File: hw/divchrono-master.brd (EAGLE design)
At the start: 100 x 80 mm, 16 parts, among them U1 TPS562200DDCR

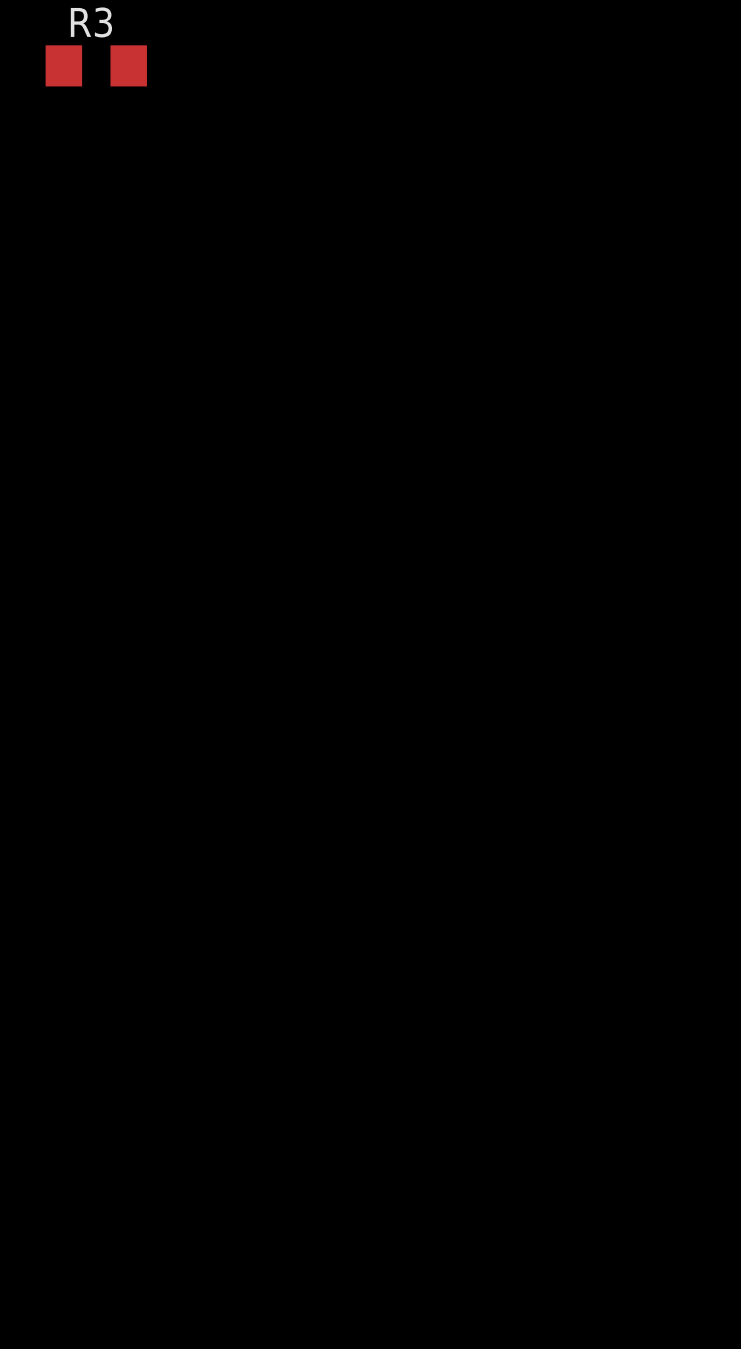
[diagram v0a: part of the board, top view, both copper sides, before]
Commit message: Added Nixie tube boost converter into schematic, library, and updated documentation for new layout.
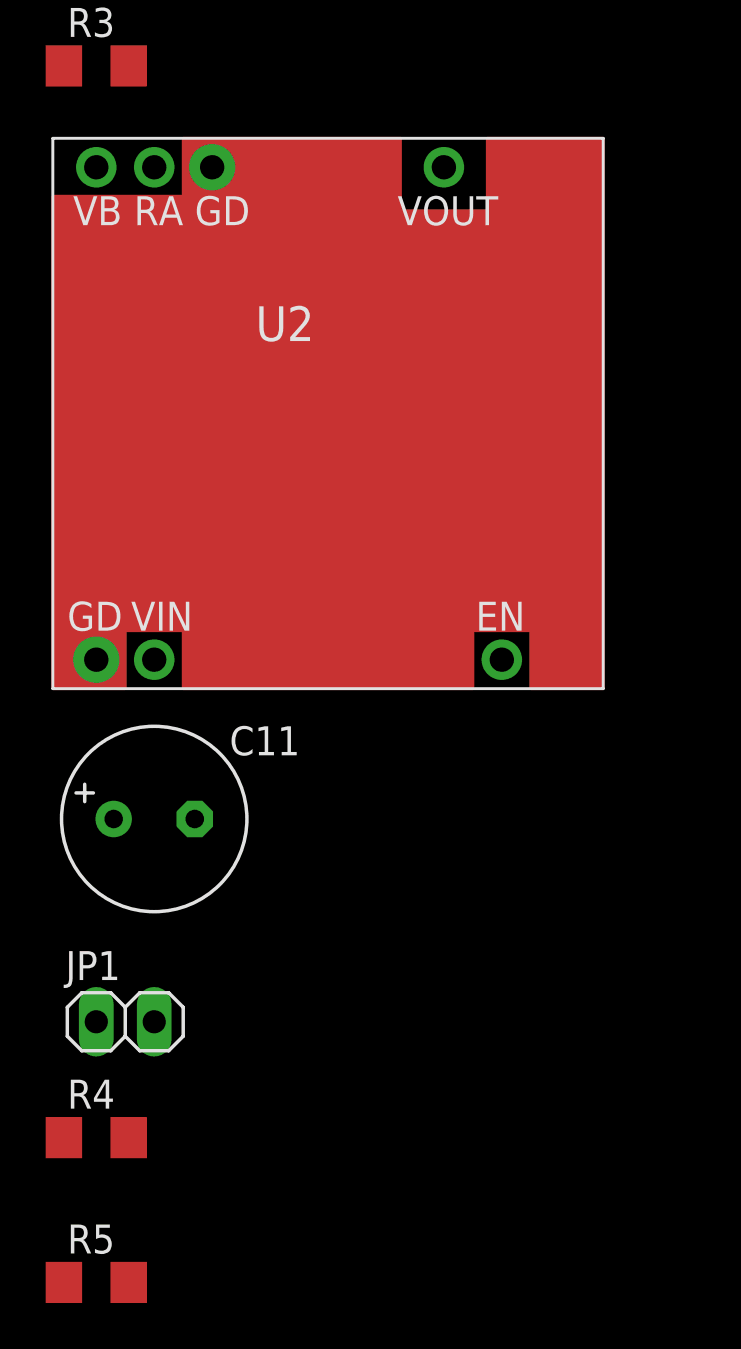
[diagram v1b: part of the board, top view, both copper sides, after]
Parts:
- added C11: 330uF, rcl:E3,5-8
- added JP1: HV, pinhead:1X02
- added R4: 100k, rcl:R1206
- added R5: 47k, rcl:R1206
- added U2: 1364, TES:1364
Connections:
- new net HV: U2.1
- new net N$3: JP1.1, R4.2, U2.7
- new net N$4: R5.2, U2.2
- net +12V: now also C11.+, JP1.2, U2.4
- net GND: now also C11.-, R4.1, R5.1, U2.3, U2.5
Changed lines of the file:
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@@
 <element name="R2" library="rcl" package="R1206" value="56k 1%" x="-29.21" y="-50.8"/>
 <element name="R3" library="rcl" package="R1206" value="10k 1%" x="-29.21" y="-55.88"/>
+<element name="U2" library="TES" package="1364" value="1364" x="-19.05" y="-71.12"/>
+<element name="C11" library="rcl" package="E3,5-8" value="330uF" x="-26.67" y="-88.9"/>
+<element name="JP1" library="pinhead" package="1X02" value="HV" x="-27.94" y="-97.79"/>
+<element name="R4" library="rcl" package="R1206" value="100k" x="-29.21" y="-102.87"/>
+<element name="R5" library="rcl" package="R1206" value="47k" x="-29.21" y="-109.22"/>
 </elements>
 <signals>
@@
 <contactref element="C4" pad="+"/>
 <contactref element="R1" pad="1"/>
-<wire x1="21.59" y1="3.81" x2="54.5846" y2="6.6802" width="0" layer="19" extent="1-1"/>
-<wire x1="-30.632" y1="34.29" x2="21.59" y2="3.81" width="0" layer="19" extent="1-1"/>
-<wire x1="-25.53" y1="34.29" x2="-30.632" y2="34.29" width="0" layer="19" extent="1-1"/>
-<wire x1="-19.18" y1="34.29" x2="-25.53" y2="34.29" width="0" layer="19" extent="1-1"/>
-<wire x1="13.97" y1="3.81" x2="-25.53" y2="34.29" width="0" layer="19" extent="1-1"/>
-<wire x1="12.57" y1="10.16" x2="21.59" y2="3.81" width="0" layer="19" extent="1-1"/>
-<wire x1="30.734" y1="3.81" x2="12.57" y2="10.16" width="0" layer="19" extent="1-1"/>
-<wire x1="5.08" y1="8.08" x2="13.97" y2="3.81" width="0" layer="19" extent="1-1"/>
+<contactref element="C11" pad="+"/>
+<contactref element="U2" pad="4"/>
+<contactref element="JP1" pad="2"/>
+<wire x1="-28.448" y1="-88.9" x2="-26.67" y2="-97.79" width="0" layer="19" extent="1-1"/>
+<wire x1="-26.67" y1="-81.915" x2="-28.448" y2="-88.9" width="0" layer="19" extent="1-1"/>
+<wire x1="13.97" y1="3.81" x2="-26.67" y2="-81.915" width="0" layer="19" extent="1-1"/>
+<wire x1="12.57" y1="10.16" x2="13.97" y2="3.81" width="0" layer="19" extent="1-1"/>
+<wire x1="21.59" y1="3.81" x2="13.97" y2="3.81" width="0" layer="19" extent="1-1"/>
+<wire x1="5.08" y1="8.08" x2="12.57" y2="10.16" width="0" layer="19" extent="1-1"/>
+<wire x1="30.734" y1="3.81" x2="21.59" y2="3.81" width="0" layer="19" extent="1-1"/>
+<wire x1="54.5846" y1="6.6802" x2="30.734" y2="3.81" width="0" layer="19" extent="1-1"/>
+<wire x1="-19.18" y1="34.29" x2="5.08" y2="8.08" width="0" layer="19" extent="1-1"/>
+<wire x1="-25.53" y1="34.29" x2="-19.18" y2="34.29" width="0" layer="19" extent="1-1"/>
+<wire x1="-30.632" y1="34.29" x2="-25.53" y2="34.29" width="0" layer="19" extent="1-1"/>
 </signal>
 <signal name="GND">
@@
 <contactref element="U1" pad="1"/>
 <contactref element="R3" pad="1"/>
+<contactref element="U2" pad="5"/>
+<contactref element="U2" pad="3"/>
+<contactref element="C11" pad="-"/>
+<contactref element="R4" pad="1"/>
+<contactref element="R5" pad="1"/>
+<wire x1="-30.632" y1="-102.87" x2="-30.632" y2="-109.22" width="0" layer="19" extent="1-1"/>
+<wire x1="-24.892" y1="-88.9" x2="-30.632" y2="-102.87" width="0" layer="19" extent="1-1"/>
+<wire x1="-29.21" y1="-81.915" x2="-24.892" y2="-88.9" width="0" layer="19" extent="1-1"/>
+<wire x1="-24.13" y1="-60.325" x2="-29.21" y2="-81.915" width="0" layer="19" extent="1-1"/>
+<wire x1="-30.632" y1="-55.88" x2="-24.13" y2="-60.325" width="0" layer="19" extent="1-1"/>
 <wire x1="-27.81" y1="-21.59" x2="-30.632" y2="-55.88" width="0" layer="19" extent="1-1"/>
 <wire x1="-27.81" y1="-15.24" x2="-27.81" y2="-21.59" width="0" layer="19" extent="1-1"/>
@@
 <wire x1="-30.61" y1="-8.89" x2="-30.61" y2="-15.24" width="0" layer="19" extent="1-1"/>
 </signal>
+<signal name="N$3">
+<contactref element="JP1" pad="1"/>
+<contactref element="U2" pad="7"/>
+<contactref element="R4" pad="2"/>
+<wire x1="-29.21" y1="-97.79" x2="-27.788" y2="-102.87" width="0" layer="19" extent="1-1"/>
+<wire x1="-11.43" y1="-81.915" x2="-29.21" y2="-97.79" width="0" layer="19" extent="1-1"/>
+</signal>
+<signal name="N$4">
+<contactref element="U2" pad="2"/>
+<contactref element="R5" pad="2"/>
+<wire x1="-26.67" y1="-60.325" x2="-27.788" y2="-109.22" width="0" layer="19" extent="1-1"/>
+</signal>
+<signal name="HV">
+<contactref element="U2" pad="1"/>
+</signal>
 </signals>

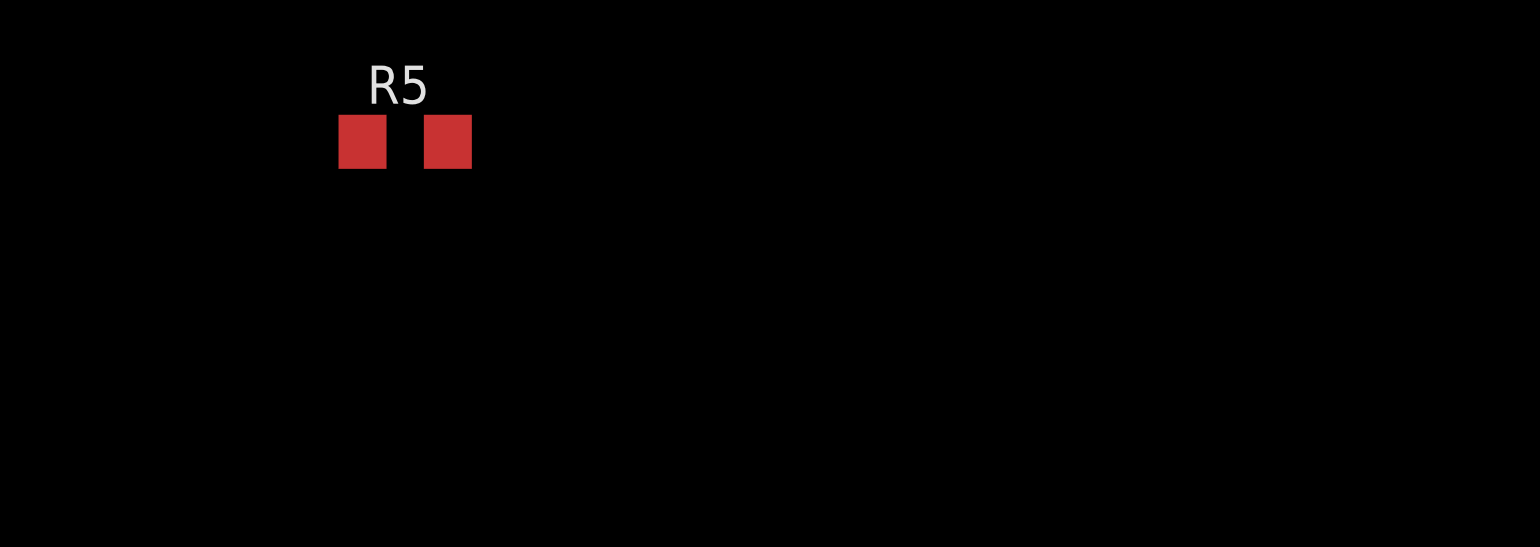
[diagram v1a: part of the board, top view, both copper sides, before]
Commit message: Mirrored pin mappings onto schematic, and fixed two small documentation errors.
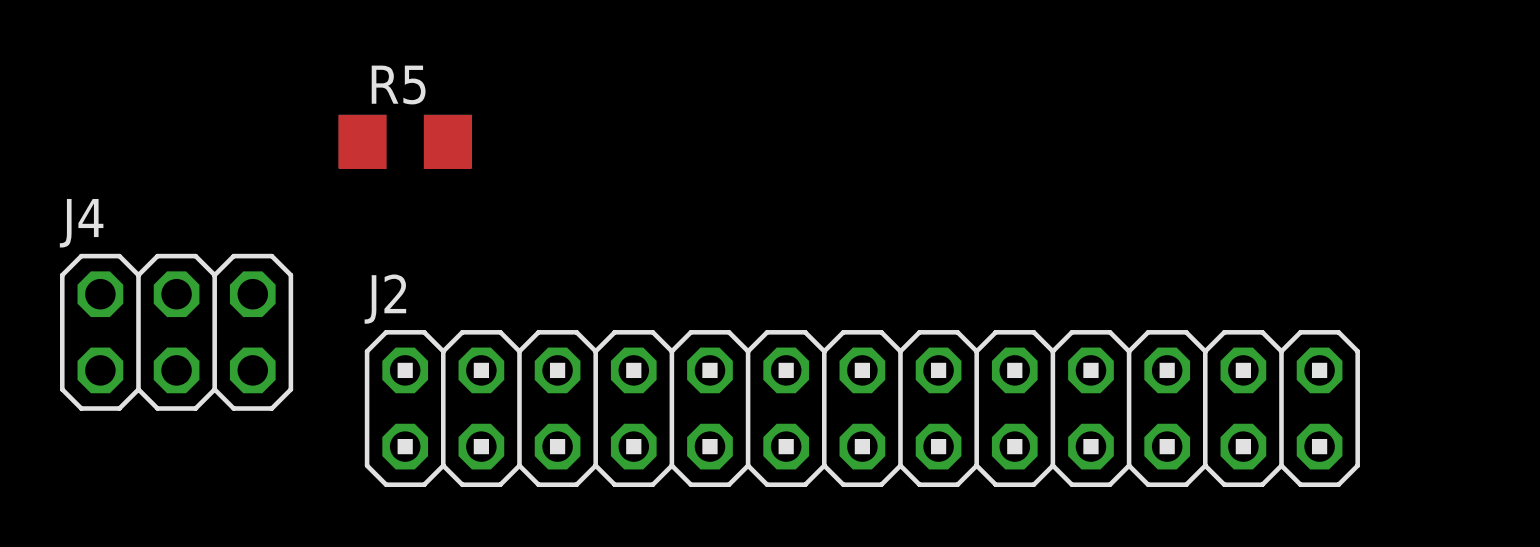
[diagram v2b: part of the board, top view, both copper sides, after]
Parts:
- added J2: (no value), pinhead:2X13
- added J4: (no value), pinhead:2X03
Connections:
- new net +3V3: J2.1, J4.2
- new net BUTTON_DOWN: J2.23
- new net BUTTON_LEFT: J2.15
- new net BUTTON_RIGHT: J2.19
- new net BUTTON_UP: J2.21
- new net DISPLAY_BLANK: J2.12
- new net DISPLAY_CLK: J2.18
- new net DISPLAY_DAT: J2.16
- new net DISPLAY_LAT: J2.10
- new net ENCODER_D1: J2.22, J4.1
- new net ENCODER_D2: J2.24, J4.3
- new net ENCODER_D3: J2.26, J4.5
- new net STATUS_CLK: J2.13
- new net STATUS_DAT: J2.11
- new net STATUS_LAT: J2.7
- net +5V: now also J2.2, J2.4
- net GND: now also J2.14, J2.20, J2.25, J2.6, J2.9, J4.6
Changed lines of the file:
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@@
 <element name="R4" library="rcl" package="R1206" value="100k" x="-29.21" y="-102.87"/>
 <element name="R5" library="rcl" package="R1206" value="47k" x="-29.21" y="-109.22"/>
+<element name="J2" library="pinhead" package="2X13" value="" x="-13.97" y="-118.11"/>
+<element name="J4" library="pinhead" package="2X03" value="" x="-36.83" y="-115.57"/>
 </elements>
 <signals>
@@
 <contactref element="R4" pad="1"/>
 <contactref element="R5" pad="1"/>
+<contactref element="J2" pad="6"/>
+<contactref element="J2" pad="14"/>
+<contactref element="J2" pad="20"/>
+<contactref element="J2" pad="25"/>
+<contactref element="J2" pad="9"/>
+<contactref element="J4" pad="6"/>
+<wire x1="-30.632" y1="-109.22" x2="-34.29" y2="-114.3" width="0" layer="19" extent="1-1"/>
 <wire x1="-30.632" y1="-102.87" x2="-30.632" y2="-109.22" width="0" layer="19" extent="1-1"/>
+<wire x1="-24.13" y1="-116.84" x2="-30.632" y2="-109.22" width="0" layer="19" extent="1-1"/>
+<wire x1="-19.05" y1="-119.38" x2="-24.13" y2="-116.84" width="0" layer="19" extent="1-1"/>
+<wire x1="-13.97" y1="-116.84" x2="-19.05" y2="-119.38" width="0" layer="19" extent="1-1"/>
+<wire x1="-6.35" y1="-116.84" x2="-13.97" y2="-116.84" width="0" layer="19" extent="1-1"/>
+<wire x1="1.27" y1="-119.38" x2="-6.35" y2="-116.84" width="0" layer="19" extent="1-1"/>
 <wire x1="-24.892" y1="-88.9" x2="-30.632" y2="-102.87" width="0" layer="19" extent="1-1"/>
 <wire x1="-29.21" y1="-81.915" x2="-24.892" y2="-88.9" width="0" layer="19" extent="1-1"/>
@@
 <contactref element="L1" pad="2"/>
 <contactref element="R2" pad="2"/>
+<contactref element="J2" pad="2"/>
+<contactref element="J2" pad="4"/>
+<wire x1="-26.67" y1="-116.84" x2="-29.21" y2="-116.84" width="0" layer="19" extent="1-1"/>
+<wire x1="-27.788" y1="-50.8" x2="-29.21" y2="-116.84" width="0" layer="19" extent="1-1"/>
 <wire x1="-22.9" y1="-35.56" x2="-27.788" y2="-50.8" width="0" layer="19" extent="1-1"/>
 <wire x1="-30.61" y1="-21.59" x2="-22.9" y2="-35.56" width="0" layer="19" extent="1-1"/>
@@
 <contactref element="U2" pad="1"/>
 </signal>
+<signal name="+3V3">
+<contactref element="J2" pad="1"/>
+<contactref element="J4" pad="2"/>
+<wire x1="-29.21" y1="-119.38" x2="-39.37" y2="-114.3" width="0" layer="19" extent="1-1"/>
+</signal>
+<signal name="STATUS_DAT">
+<contactref element="J2" pad="11"/>
+</signal>
+<signal name="STATUS_LAT">
+<contactref element="J2" pad="7"/>
+</signal>
+<signal name="STATUS_CLK">
+<contactref element="J2" pad="13"/>
+</signal>
+<signal name="DISPLAY_DAT">
+<contactref element="J2" pad="16"/>
+</signal>
+<signal name="DISPLAY_CLK">
+<contactref element="J2" pad="18"/>
+</signal>
+<signal name="ENCODER_D1">
+<contactref element="J2" pad="22"/>
+<contactref element="J4" pad="1"/>
+<wire x1="-3.81" y1="-116.84" x2="-39.37" y2="-116.84" width="0" layer="19" extent="1-1"/>
+</signal>
+<signal name="DISPLAY_BLANK">
+<contactref element="J2" pad="12"/>
+</signal>
+<signal name="BUTTON_LEFT">
+<contactref element="J2" pad="15"/>
+</signal>
+<signal name="BUTTON_RIGHT">
+<contactref element="J2" pad="19"/>
+</signal>
+<signal name="BUTTON_UP">
+<contactref element="J2" pad="21"/>
+</signal>
+<signal name="BUTTON_DOWN">
+<contactref element="J2" pad="23"/>
+</signal>
+<signal name="ENCODER_D2">
+<contactref element="J2" pad="24"/>
+<contactref element="J4" pad="3"/>
+<wire x1="-1.27" y1="-116.84" x2="-36.83" y2="-116.84" width="0" layer="19" extent="1-1"/>
+</signal>
+<signal name="ENCODER_D3">
+<contactref element="J2" pad="26"/>
+<contactref element="J4" pad="5"/>
+<wire x1="1.27" y1="-116.84" x2="-34.29" y2="-116.84" width="0" layer="19" extent="1-1"/>
+</signal>
+<signal name="DISPLAY_LAT">
+<contactref element="J2" pad="10"/>
+</signal>
 </signals>

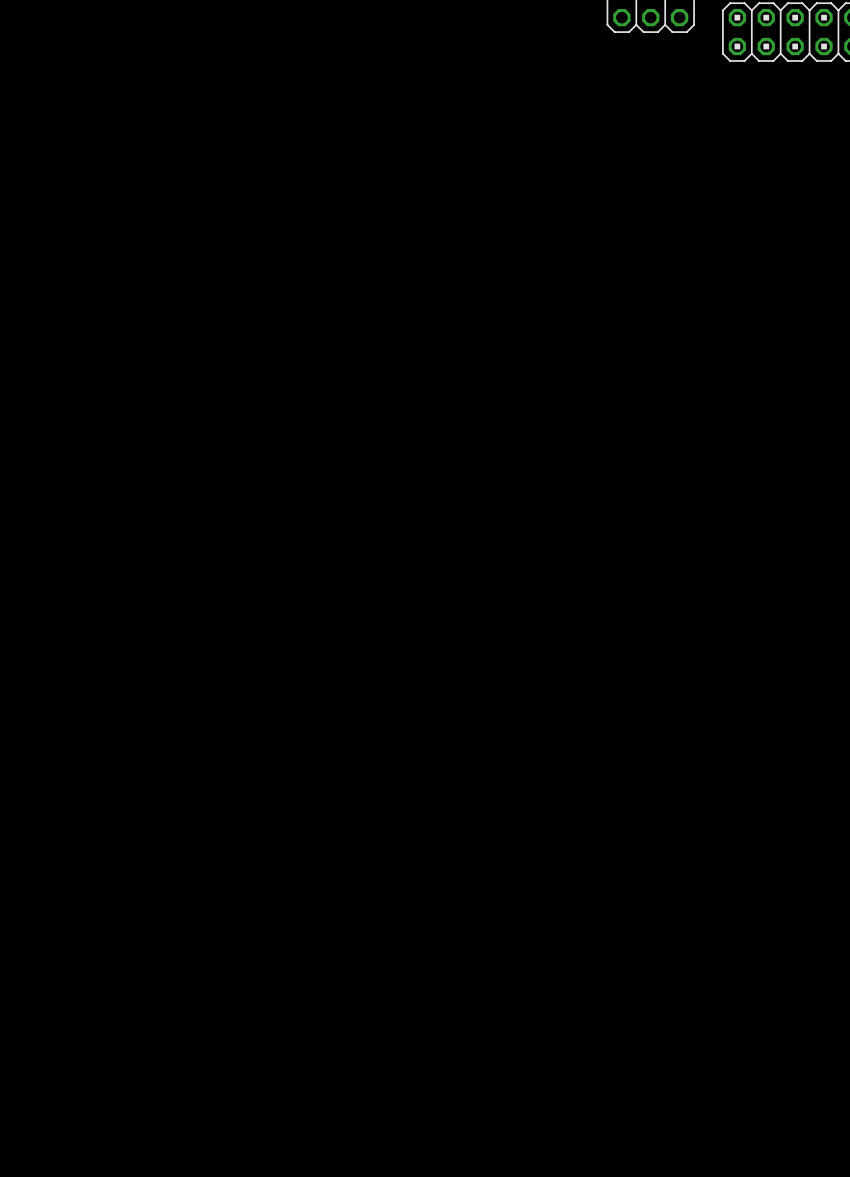
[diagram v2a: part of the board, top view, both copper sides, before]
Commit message: Laid out major board connections/pin mappings, and started on framework for encoder and amplifier boards. Minor documentation updates to reflect changes.
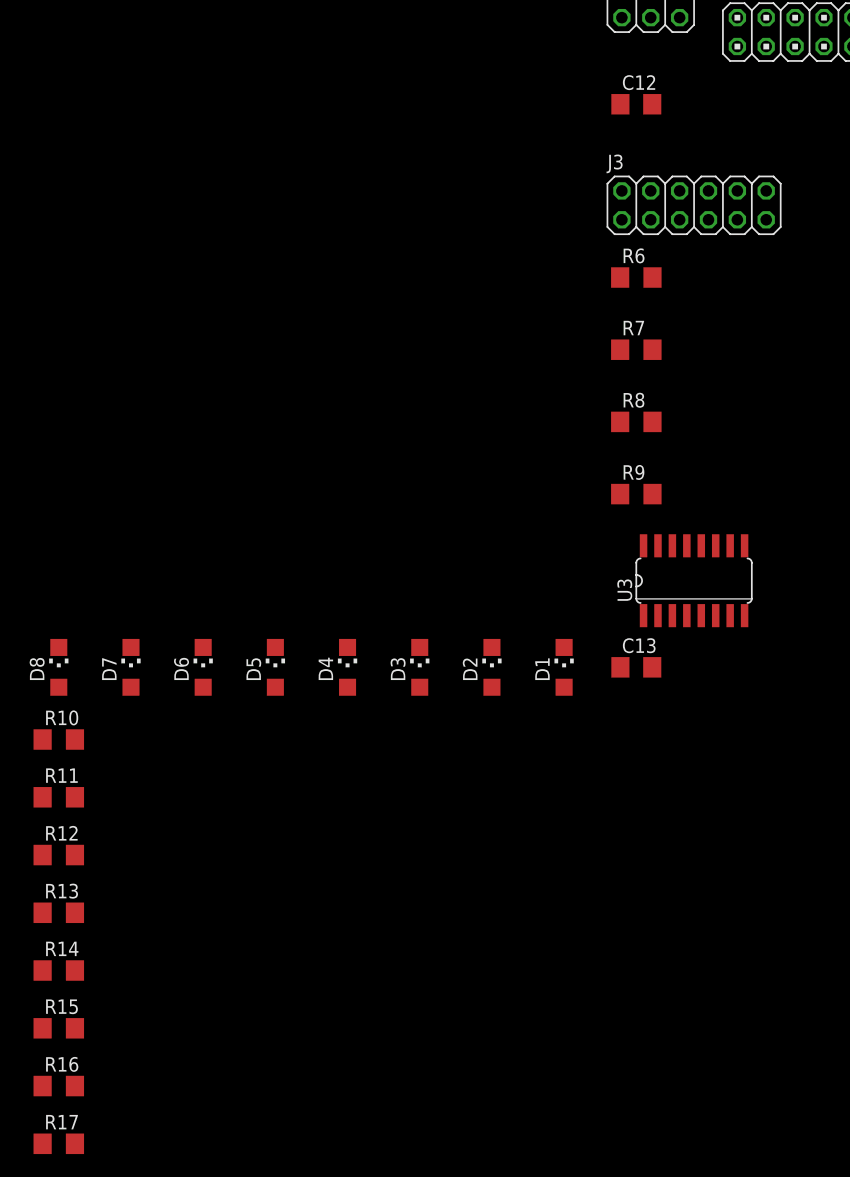
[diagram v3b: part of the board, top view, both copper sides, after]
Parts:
- added C12, C13: 100nF, rcl:C1206
- added D1, D2, D3, D4, D5, D6, D7, D8: (no value), led:CHIPLED_1206
- added J3: (no value), pinhead:2X06
- added R10, R11, R12, R13, R14, R15, R16, R17: 1k, rcl:R1206
- added R6, R7, R8, R9: 10k, rcl:R1206
- added U3: 74HC595D, 74xx-eu:SO16
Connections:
- new net N$10: J3.3
- new net N$11: J3.5
- new net N$12: J3.7
- new net N$13: J3.9
- new net N$14: D2.A, U3.1
- new net N$15: D1.A, U3.15
- new net N$16: D6.A, U3.5
- new net N$17: D7.A, U3.6
- new net N$18: D8.A, U3.7
- new net N$19: D1.C, R10.1
- new net N$20: D2.C, R11.1
- new net N$21: D3.C, R12.1
- new net N$22: D4.C, R13.1
- new net N$23: D5.C, R14.1
- new net N$24: D6.C, R15.1
- new net N$25: D7.C, R16.1
- new net N$26: D8.C, R17.1
- new net N$7: D5.A, U3.4
- new net N$8: D4.A, U3.3
- new net N$9: D3.A, U3.2
- net +12V: now also J3.2
- net +3V3: now also C12.1, C13.1, J2.17, R6.2, R7.2, R8.2, R9.2, U3.10, U3.16
- net BUTTON_DOWN: now also J3.10, R9.1
- net BUTTON_LEFT: now also J3.4, R6.1
- net BUTTON_RIGHT: now also J3.6, R7.1
- net BUTTON_UP: now also J3.8, R8.1
- net GND: now also C12.2, C13.2, J3.11, J3.12, R10.2, R11.2, R12.2, R13.2, R14.2, R15.2, R16.2, R17.2, U3.13, U3.8
- net HV: now also J3.1
- net STATUS_CLK: now also U3.11
- net STATUS_DAT: now also U3.14
- net STATUS_LAT: now also U3.12
